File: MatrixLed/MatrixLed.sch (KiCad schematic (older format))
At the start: 64 parts

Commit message: Matriz terminada
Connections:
- wire segments 43 -> 80
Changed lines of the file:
@@
 	9100 1800 9300 1800
 Connection ~ 9300 1800
+Wire Wire Line
+	7700 1800 7850 1800
+Connection ~ 7850 1800
+Wire Wire Line
+	7350 1800 7500 1800
+Connection ~ 7500 1800
+Wire Wire Line
+	7000 1800 7150 1800
+Connection ~ 7150 1800
+Wire Wire Line
+	6650 1800 6800 1800
+Connection ~ 6800 1800
+Wire Wire Line
+	6650 2250 6800 2250
+Connection ~ 6800 2250
+Wire Wire Line
+	7000 2250 7150 2250
+Connection ~ 7150 2250
+Wire Wire Line
+	7350 2250 7500 2250
+Connection ~ 7500 2250
+Wire Wire Line
+	7700 2250 7850 2250
+Connection ~ 7850 2250
+Wire Wire Line
+	7700 2700 7850 2700
+Connection ~ 7850 2700
+Wire Wire Line
+	7350 2700 7500 2700
+Connection ~ 7500 2700
+Wire Wire Line
+	7000 2700 7150 2700
+Connection ~ 7150 2700
+Wire Wire Line
+	7000 3150 7150 3150
+Connection ~ 7150 3150
+Wire Wire Line
+	7350 3150 7500 3150
+Connection ~ 7500 3150
+Wire Wire Line
+	7700 3150 7850 3150
+Connection ~ 7850 3150
+Wire Wire Line
+	8050 3150 8200 3150
+Connection ~ 8200 3150
+Wire Wire Line
+	9100 4500 9300 4500
+Connection ~ 9300 4500
+Wire Wire Line
+	8750 4500 8900 4500
+Connection ~ 8900 4500
+Wire Wire Line
+	8400 4500 8550 4500
+Connection ~ 8550 4500
+Wire Wire Line
+	8050 4500 8200 4500
+Connection ~ 8200 4500
+Wire Wire Line
+	7700 4500 7850 4500
+Connection ~ 7850 4500
+Wire Wire Line
+	7350 4500 7500 4500
+Connection ~ 7500 4500
+Wire Wire Line
+	7000 4500 7150 4500
+Connection ~ 7150 4500
+Wire Wire Line
+	6650 4500 6800 4500
+Connection ~ 6800 4500
+Wire Wire Line
+	6650 4950 6800 4950
+Wire Wire Line
+	7000 4950 7150 4950
+Wire Wire Line
+	7350 4950 7500 4950
+Wire Wire Line
+	7700 4950 7850 4950
+Wire Wire Line
+	7700 4050 7850 4050
+Connection ~ 7850 4050
+Wire Wire Line
+	7350 4050 7500 4050
+Connection ~ 7500 4050
+Wire Wire Line
+	7000 4050 7150 4050
+Connection ~ 7150 4050
+Wire Wire Line
+	6650 4050 6800 4050
+Connection ~ 6800 4050
+Wire Wire Line
+	6650 3150 6800 3150
+Connection ~ 6800 3150
+Wire Wire Line
+	6650 2700 6800 2700
+Connection ~ 6800 2700
+Wire Wire Line
+	6650 3600 6800 3600
+Connection ~ 6800 3600
+Wire Wire Line
+	7000 3600 7150 3600
+Connection ~ 7150 3600
+Wire Wire Line
+	7350 3600 7500 3600
+Connection ~ 7500 3600
+Wire Wire Line
+	7700 3600 7850 3600
+Connection ~ 7850 3600
 $EndSCHEMATC

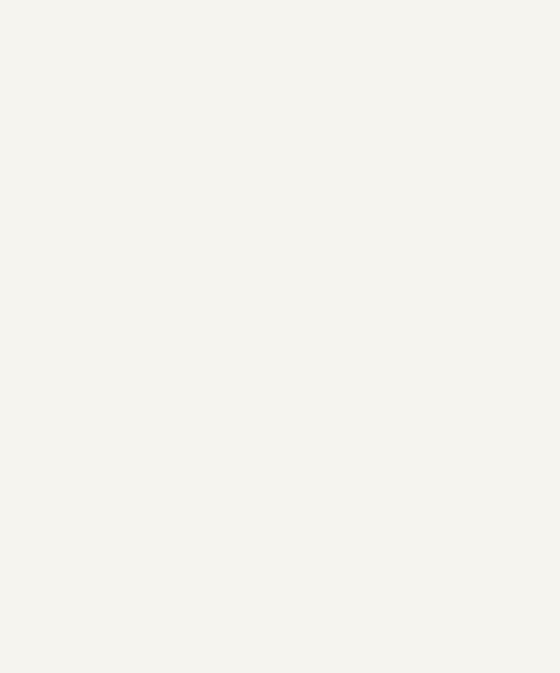
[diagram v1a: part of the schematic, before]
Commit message: Max7219 añadido
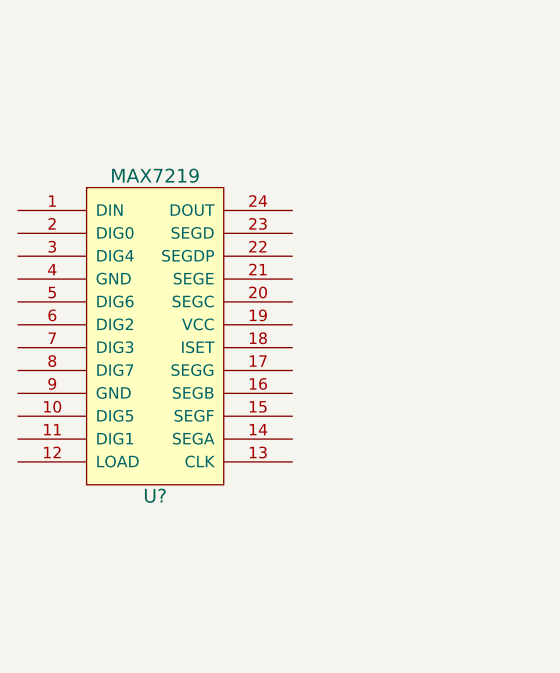
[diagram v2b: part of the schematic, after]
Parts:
- added U?: MAX7219, symbol MAX7219
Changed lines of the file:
@@
 LIBS:contrib
 LIBS:valves
+LIBS:74xgxx
+LIBS:ac-dc
+LIBS:actel
+LIBS:allegro
+LIBS:Altera
+LIBS:analog_devices
+LIBS:battery_management
+LIBS:bbd
+LIBS:bosch
+LIBS:brooktre
+LIBS:cmos_ieee
+LIBS:dc-dc
+LIBS:diode
+LIBS:elec-unifil
+LIBS:ESD_Protection
+LIBS:ftdi
+LIBS:gennum
+LIBS:graphic
+LIBS:hc11
+LIBS:ir
+LIBS:L9110
+LIBS:Lattice
+LIBS:logo
+LIBS:maxim
+LIBS:mechanical
+LIBS:microchip_dspic33dsc
+LIBS:microchip_pic10mcu
+LIBS:microchip_pic12mcu
+LIBS:microchip_pic16mcu
+LIBS:microchip_pic18mcu
+LIBS:microchip_pic32mcu
+LIBS:motor_drivers
+LIBS:motors
+LIBS:msp430
+LIBS:nordicsemi
+LIBS:nxp_armmcu
+LIBS:onsemi
+LIBS:Oscillators
+LIBS:powerint
+LIBS:Power_Management
+LIBS:pspice
+LIBS:references
+LIBS:relays
+LIBS:rfcom
+LIBS:sensors
+LIBS:silabs
+LIBS:stm8
+LIBS:stm32
+LIBS:supertex
+LIBS:switches
+LIBS:transf
+LIBS:ttl_ieee
+LIBS:video
+LIBS:wiznet
+LIBS:Worldsemi
+LIBS:Xicor
+LIBS:zetex
+LIBS:Zilog
+LIBS:max
 LIBS:MatrixLed-cache
 EELAYER 25 0
@@
 	7700 3600 7850 3600
 Connection ~ 7850 3600
+$Comp
+L MAX7219 U?
+U 1 1 58F6F327
+P 3450 3000
+F 0 "U?" H 3450 2300 60  0000 C CNN
+F 1 "MAX7219" H 3450 3700 60  0000 C CNN
+F 2 "" H 4050 3000 60  0000 C CNN
+F 3 "" H 4050 3000 60  0000 C CNN
+	1    3450 3000
+	1    0    0    -1
+$EndComp
 $EndSCHEMATC

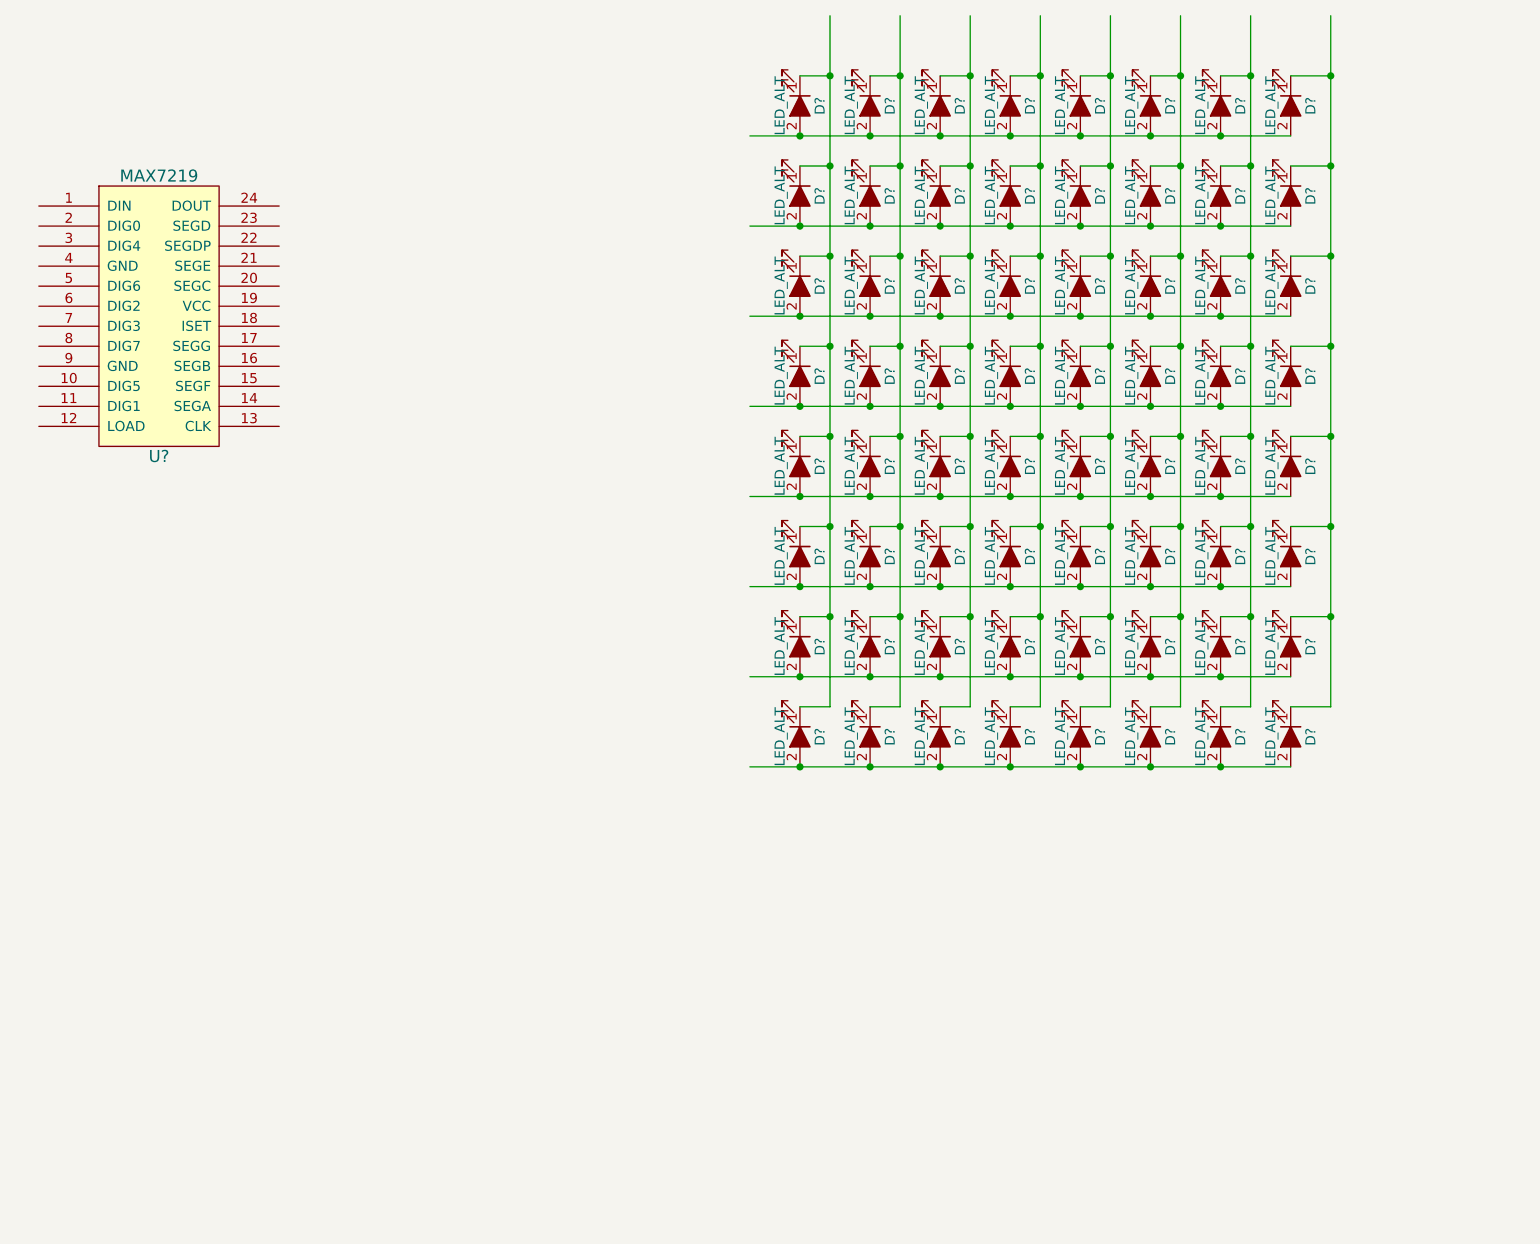
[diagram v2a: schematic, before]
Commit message: MAX7219 conectado con la matriz
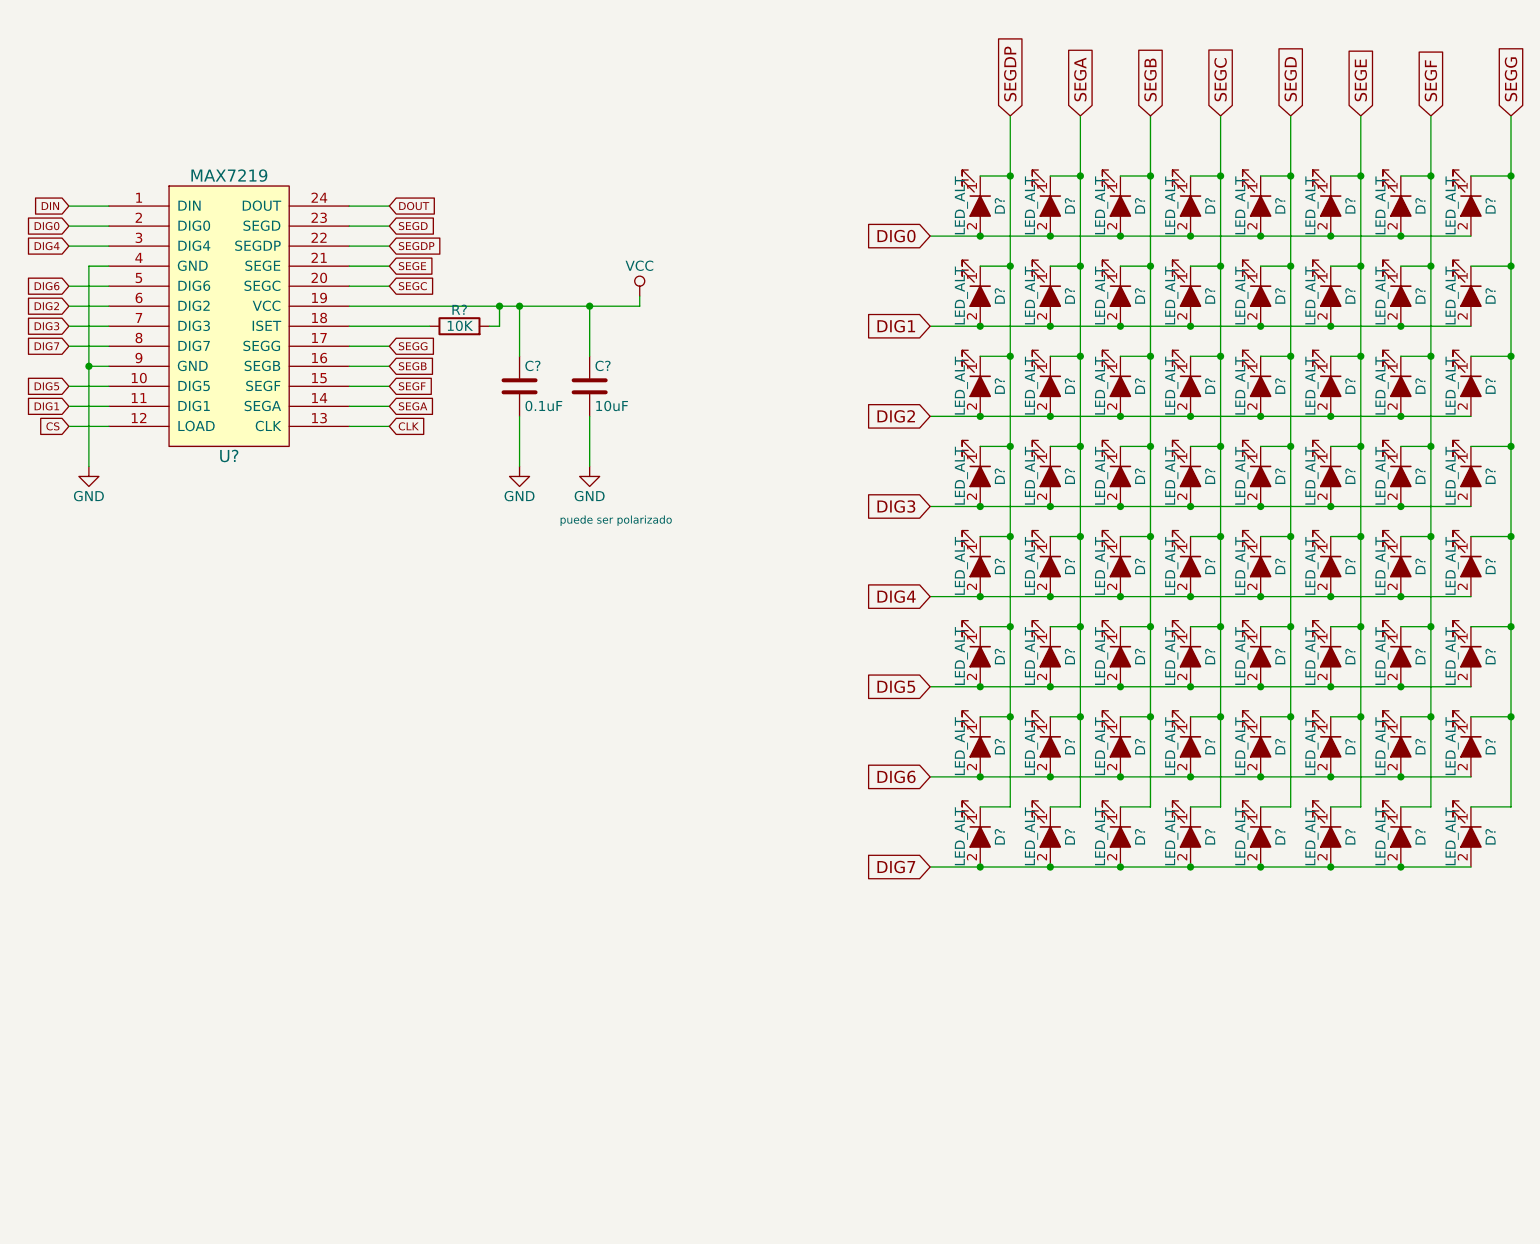
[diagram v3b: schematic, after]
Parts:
- added C?: 10uF, symbol C
- added C?: 0.1uF, symbol C
- added R?: 10K, symbol R
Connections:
- net labels added: CLK, CS, DIG0, DIG1, DIG2, DIG3, DIG4, DIG5, DIG6, DIG7, DIN, DOUT, GND, SEGA, SEGB, SEGC, SEGD, SEGDP, SEGE, SEGF, SEGG, VCC
- wire segments 80 -> 112
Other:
- note added: "puede ser polarizado\n"
- moved on the sheet: D?, U?

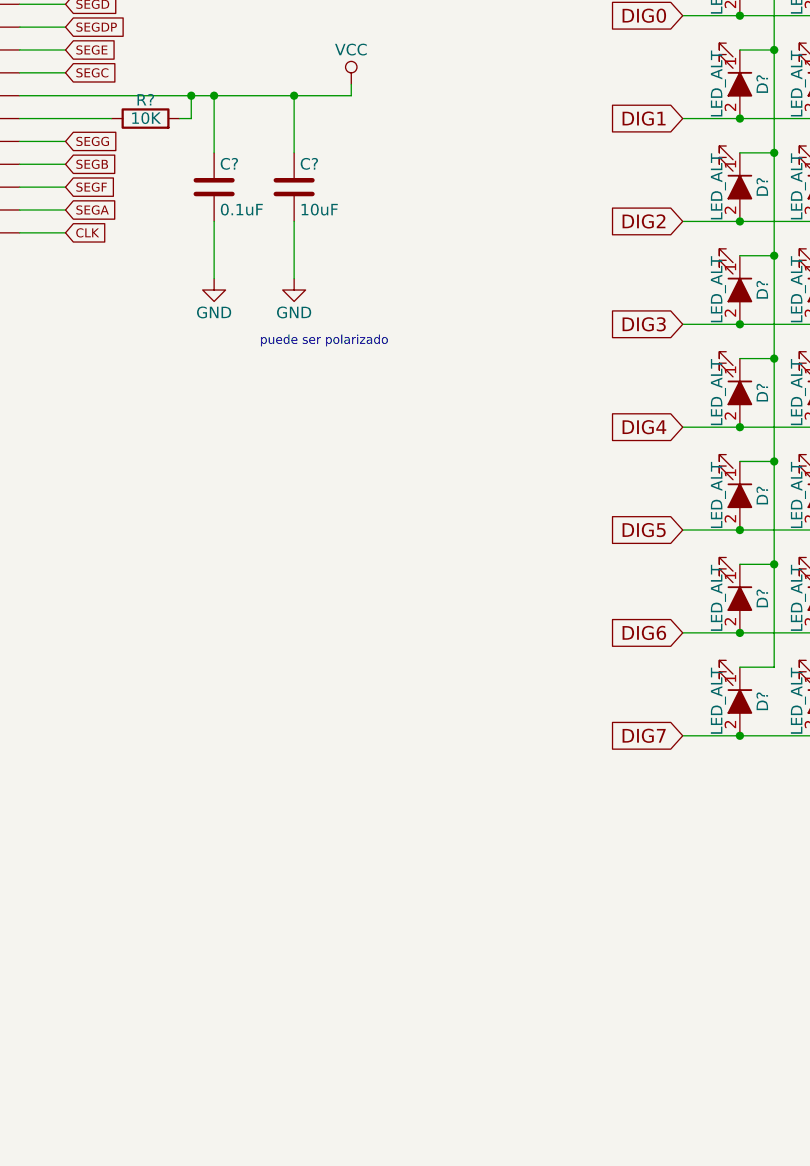
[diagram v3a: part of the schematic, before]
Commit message: Power flags añadidos
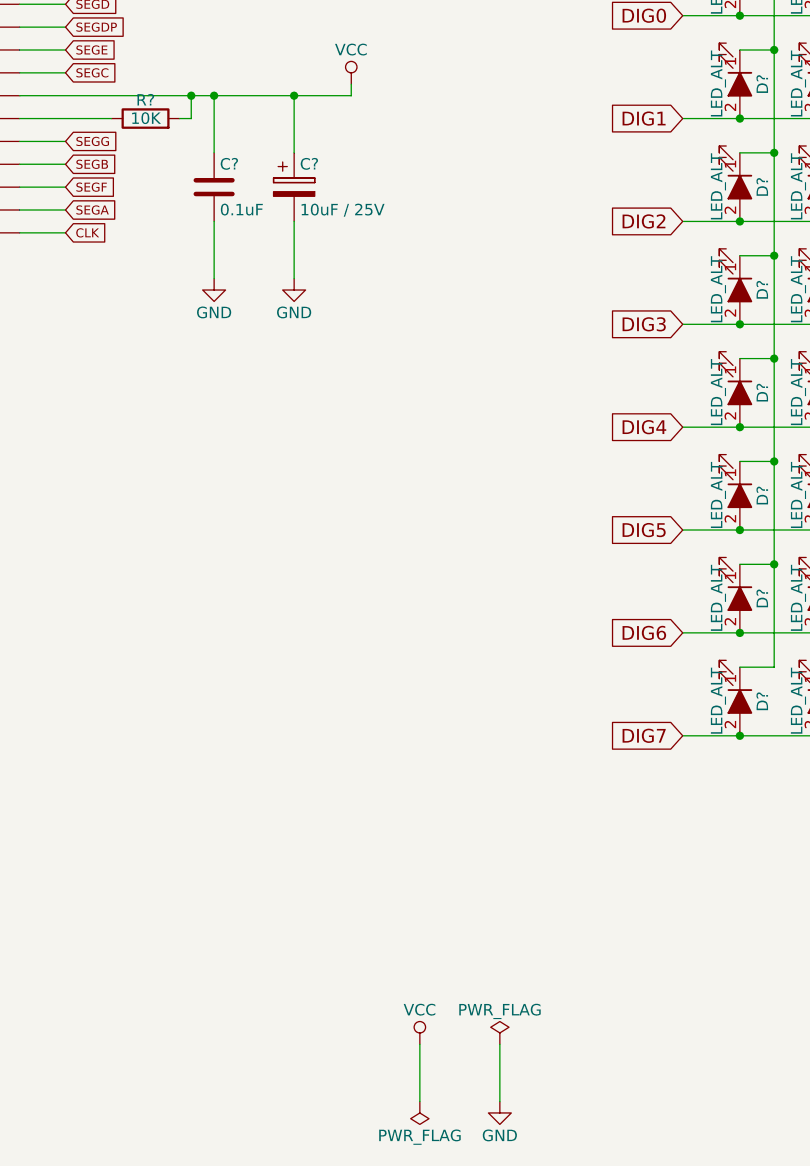
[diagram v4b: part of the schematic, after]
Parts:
- removed C?: 10uF, symbol C
- added C?: 10uF / 25V, symbol CP
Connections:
- net GND: now also C?.2
- net VCC: now also C?.1
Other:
- note removed: "puede ser polarizado\n"
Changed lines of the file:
@@
 DIG1
-$Comp
-L C C?
-U 1 1 58F7D266
-P 5600 3350
-F 0 "C?" H 5625 3450 50  0000 L CNN
-F 1 "10uF" H 5625 3250 50  0000 L CNN
-F 2 "" H 5638 3200 50  0001 C CNN
-F 3 "" H 5600 3350 50  0001 C CNN
-	1    5600 3350
-	1    0    0    -1
-$EndComp
 $Comp
 L R R?
@@
 	5600 2950 5600 3200
 Connection ~ 5250 2950
-Text Notes 5450 4050 0    39   ~ 0
-puede ser polarizado\n
 $Comp
 L VCC #PWR?
@@
 Text GLabel 3000 3550 0    39   Input ~ 0
 CS
+$Comp
+L CP C?
+U 1 1 58F8BEE2
+P 5600 3350
+F 0 "C?" H 5625 3450 50  0000 L CNN
+F 1 "10uF / 25V" H 5625 3250 50  0000 L CNN
+F 2 "" H 5638 3200 50  0001 C CNN
+F 3 "" H 5600 3350 50  0001 C CNN
+	1    5600 3350
+	1    0    0    -1
+$EndComp
+$Comp
+L PWR_FLAG #FLG?
+U 1 1 58F8D180
+P 6500 7100
+F 0 "#FLG?" H 6500 7175 50  0001 C CNN
+F 1 "PWR_FLAG" H 6500 7250 50  0000 C CNN
+F 2 "" H 6500 7100 50  0001 C CNN
+F 3 "" H 6500 7100 50  0001 C CNN
+	1    6500 7100
+	1    0    0    -1
+$EndComp
+$Comp
+L PWR_FLAG #FLG?
+U 1 1 58F8D47E
+P 6150 7350
+F 0 "#FLG?" H 6150 7425 50  0001 C CNN
+F 1 "PWR_FLAG" H 6150 7500 50  0000 C CNN
+F 2 "" H 6150 7350 50  0001 C CNN
+F 3 "" H 6150 7350 50  0001 C CNN
+	1    6150 7350
+	-1   0    0    1
+$EndComp
+$Comp
+L GND #PWR?
+U 1 1 58F8DAA5
+P 6500 7350
+F 0 "#PWR?" H 6500 7100 50  0001 C CNN
+F 1 "GND" H 6500 7200 50  0000 C CNN
+F 2 "" H 6500 7350 50  0001 C CNN
+F 3 "" H 6500 7350 50  0001 C CNN
+	1    6500 7350
+	1    0    0    -1
+$EndComp
+$Comp
+L VCC #PWR?
+U 1 1 58F8E72C
+P 6150 7100
+F 0 "#PWR?" H 6150 6950 50  0001 C CNN
+F 1 "VCC" H 6150 7250 50  0000 C CNN
+F 2 "" H 6150 7100 50  0001 C CNN
+F 3 "" H 6150 7100 50  0001 C CNN
+	1    6150 7100
+	1    0    0    -1
+$EndComp
+Wire Wire Line
+	6150 7100 6150 7350
+Wire Wire Line
+	6500 7350 6500 7100
 $EndSCHEMATC
